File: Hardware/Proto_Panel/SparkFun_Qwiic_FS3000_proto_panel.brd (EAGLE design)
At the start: 25.4 x 25.4 mm, 58 parts, among them J2 QWIIC_RA, J3 QWIIC_RA, U1 FS3000

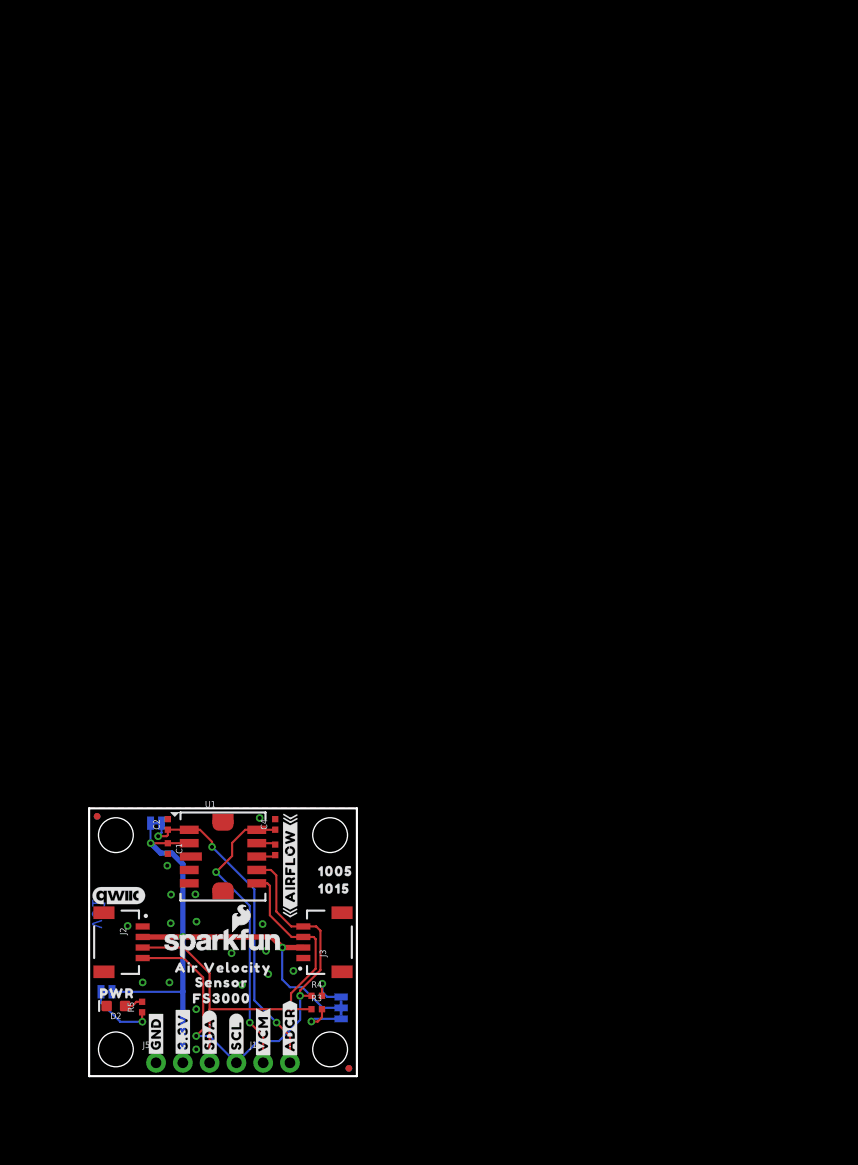
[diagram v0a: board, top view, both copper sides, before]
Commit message: Proto panel and gerbers
-Made a proto panel that includes 3 copies of each design. This allows us to order a single stencil and saves production time when building 3 prototype copies of each (1X1 and TEE) by hand.
-note, I had to move the VCM and ADCR buzzard labels on the 1x1 to a separate library, so I could drop it into the "proto panel" without it updating/breaking the other design.
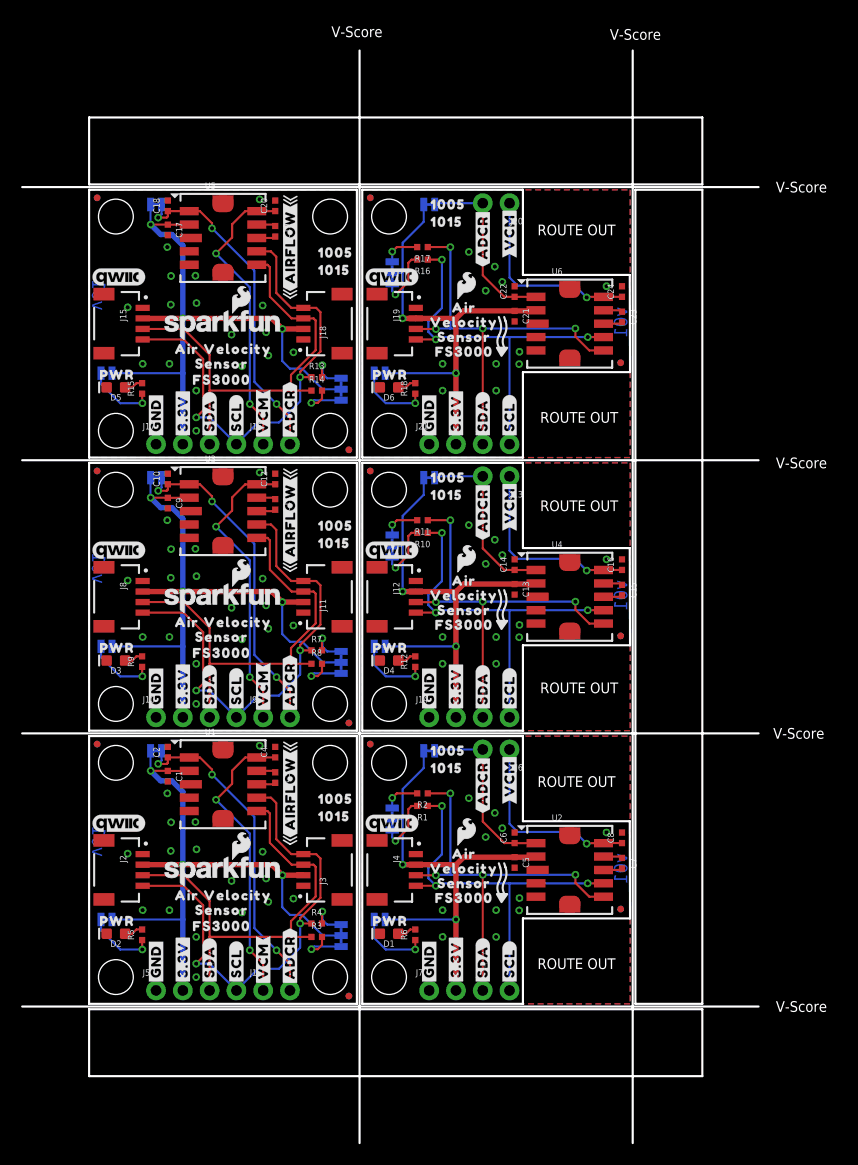
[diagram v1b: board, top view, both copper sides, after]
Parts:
- removed FRAME1: FRAME-LETTER, SparkFun-Aesthetics:CREATIVE_COMMONS
- added ADC-REF1, ADC-REF2, ADC-REF3, ADC-REF4, ADC-REF5: (no value), SparkFun-Jumpers:SMT-JUMPER_2_NC_TRACE_SILK
- added C10, C11, C13, C14, C15, C17, C18, C19, C21, C22, C23, C5, C6, C7, C9: 0.1uF, SparkFun-Capacitors:0402-TIGHT
- added C12, C16, C20, C24, C8: 1.0uF, SparkFun-Capacitors:0402-TIGHT
- added D1, D3, D4, D5, D6: RED, SparkFun-LED:LED-0603
- added I2C1, I2C2, I2C3, I2C4, I2C5: (no value), SparkFun-Jumpers:SMT-JUMPER_3_2-NC_TRACE_SILK
- added J10, J14, J17, J21, J7: (no value), SparkFun-Connectors:1X04_NO_SILK
- added J11, J12, J15, J18, J19, J4, J8: QWIIC_RA, SparkFun-Connectors:JST04_1MM_RA
- added J13, J16, J20, J6, J9: (no value), SparkFun-Connectors:1X02_NO_SILK
- added JP10, JP12, JP13, JP14, JP18, JP19, JP20, JP21, JP27, JP28, JP29, JP30, JP34, JP35, JP36, JP37, JP43, JP44, JP45, JP46: FIDUCIALUFIDUCIAL, SparkFun-Aesthetics:FIDUCIAL-MICRO
- added JP15, JP17, JP22, JP24, JP25, JP26, JP31, JP33, JP38, JP40, JP41, JP42, JP47, JP9: STAND-OFF, SparkFun-Hardware:STAND-OFF
- added JP16, JP23, JP32, JP39, JP48: LED, SparkFun-Jumpers:SMT-JUMPER_2_NC_TRACE_SILK
- added LOGO10, LOGO14, LOGO18, LOGO22, LOGO6: QWIIC_LOGO_5MM, SparkFun-Aesthetics:QWIIC_5MM
- added LOGO11, LOGO12, LOGO16, LOGO19, LOGO20, LOGO24, LOGO8: SFE_LOGO_NAME_FLAME.1_INCH, SparkFun-Aesthetics:SFE_LOGO_NAME_FLAME_.1
- added LOGO13, LOGO17, LOGO2, LOGO21, LOGO9: OSHW-LOGOMINI, SparkFun-Aesthetics:OSHW-LOGO-MINI
- added LOGO15, LOGO23, LOGO7: SFE_LOGO_FLAME.1_INCH, SparkFun-Aesthetics:SFE_LOGO_FLAME_.1
- added R1, R10, R11, R13, R14, R16, R17, R2, R7, R8: 2.2k, SparkFun-Resistors:0402-TIGHT
- added R12, R15, R18, R6, R9: 1k, SparkFun-Resistors:0402-TIGHT
- added U$1, U$113, U$114, U$142, U$143, U$2, U$57, U$58, U$86, U$87: (no value), output:#GND#0
- added U$100, U$152, U$156, U$40, U$44, U$96: (no value), output:#ADCR#0
- added U$101, U$106, U$124, U$129, U$157, U$162, U$45, U$50, U$68, U$73: (no value), output:FS30001
- added U$102, U$107, U$125, U$130, U$158, U$163, U$46, U$51, U$69, U$74: (no value), output:VELOCITY30003
- added U$103, U$108, U$126, U$131, U$159, U$164, U$47, U$52, U$70, U$75: (no value), output:AIR30004
- added U$104, U$109, U$127, U$132, U$160, U$165, U$48, U$53, U$71, U$76: (no value), output:SENSOR30005
- added U$105, U$128, U$161, U$49, U$72: (no value), output:#ADC#REF#0
- added U$110, U$136, U$166, U$54, U$80: (no value), output:10050
- added U$111, U$137, U$167, U$55, U$81: (no value), output:10150
- added U$112, U$168, U$56: (no value), output:I2C_ADR#_0X280
- added U$115, U$116, U$144, U$145, U$32, U$33, U$59, U$60, U$88, U$89: (no value), output:#3#3V#0
- added U$117, U$123, U$146, U$154, U$34, U$42, U$61, U$67, U$90, U$98: (no value), output:#SDA#0
- added U$118, U$122, U$147, U$153, U$35, U$41, U$62, U$66, U$91, U$97: (no value), output:#SCL#0
- added U$119, U$148, U$36, U$63, U$92: (no value), output:#LED#0
- added U$120, U$149, U$37, U$64, U$93: (no value), output:PWR0
- added U$121, U$150, U$38, U$65, U$94: (no value), output:#I2C#0
- added U$133, U$134, U$77, U$78: (no value), output:#AIRFLOW#0
- added U$135, U$79: (no value), output:I2C_ADD#_0X280
- added U$138, U$139, U$82, U$83: (no value), FS3000:#ADCR#4
- added U$140, U$141, U$84, U$85: (no value), FS3000:#VCM#3
- added U$151, U$155, U$39, U$43, U$95, U$99: (no value), output:#VCM#0
- added U2, U3, U4, U5, U6: FS3000, FS3000:FS3000
- moved U$28 6.86 mm to (19.2, 20.6)
- moved ADC-REF 6.86 mm to (6.35, 30.9)
- moved C1 6.86 mm to (7.47, 28.4)
- moved C2 6.86 mm to (7.47, 30.7)
- moved C3 6.86 mm to (17.7, 28.3)
- moved C4 6.86 mm to (17.7, 30.7)
- moved D2 6.86 mm to (2.54, 13.5)
- moved I2C 6.86 mm to (23.9, 13.3)
- moved J1 6.86 mm to (16.5, 8.13)
- moved J2 6.86 mm to (5.08, 19.6)
- moved J3 6.86 mm to (20.3, 19.6)
- moved J5 6.86 mm to (6.35, 8.13)
- moved JP1 6.86 mm to (1.65, 14.9)
- moved JP3 6.86 mm to (2.54, 29.7)
- moved JP4 6.86 mm to (22.9, 29.7)
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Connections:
- new net 3.3V1: ADC-REF1.1, C5.1, I2C1.2, J4.2, J7.2, JP16.2, U2.2
- new net 3.3V2: ADC-REF2.1, C9.1, I2C2.2, J10.2, J11.2, J8.2, JP23.2, U3.2
- new net 3.3V3: ADC-REF3.1, C13.1, I2C3.2, J12.2, J14.2, JP32.2, U4.2
- new net 3.3V4: ADC-REF4.1, C17.1, I2C4.2, J15.2, J17.2, J18.2, JP39.2, U5.2
- new net 3.3V5: ADC-REF5.1, C21.1, I2C5.2, J19.2, J21.2, JP48.2, U6.2
- new net ADC-REF1: ADC-REF1.2, C6.1, J6.2, U2.1
- new net ADC-REF2: ADC-REF2.2, C10.1, J9.2, U3.1
- new net ADC-REF3: ADC-REF3.2, C14.1, J13.2, U4.1
- new net ADC-REF4: ADC-REF4.2, C18.1, J16.2, U5.1
- new net ADC-REF5: ADC-REF5.2, C22.1, J20.2, U6.1
- new net GND1: C5.2, C6.2, C8.2, D1.C, J4.1, J7.1, U2.3
- new net GND2: C10.2, C12.2, C9.2, D3.C, J10.1, J11.1, J8.1, U3.3
- new net GND3: C13.2, C14.2, C16.2, D4.C, J12.1, J14.1, U4.3
- new net GND4: C17.2, C18.2, C20.2, D5.C, J15.1, J17.1, J18.1, U5.3
- new net GND5: C21.2, C22.2, C24.2, D6.C, J19.1, J21.1, U6.3
- new net N$10: JP16.1, R6.1
- new net N$11: C7.1, U2.9
- new net N$12: C7.2, U2.8
- new net N$13: I2C2.1, R8.2
- new net N$14: I2C2.3, R7.2
- new net N$15: D3.A, R9.2
- new net N$16: JP23.1, R9.1
- new net N$17: C11.1, U3.9
- new net N$18: C11.2, U3.8
- new net N$19: I2C3.1, R11.2
- new net N$20: I2C3.3, R10.2
- new net N$21: D4.A, R12.2
- new net N$22: JP32.1, R12.1
- new net N$23: C15.1, U4.9
- new net N$24: C15.2, U4.8
- new net N$25: I2C4.1, R14.2
- new net N$26: I2C4.3, R13.2
- new net N$27: D5.A, R15.2
- new net N$28: JP39.1, R15.1
- new net N$29: C19.1, U5.9
- new net N$30: C19.2, U5.8
- new net N$31: I2C5.1, R17.2
- new net N$32: I2C5.3, R16.2
- new net N$33: D6.A, R18.2
- new net N$34: JP48.1, R18.1
- new net N$35: C23.1, U6.9
- new net N$36: C23.2, U6.8
- new net N$5: I2C1.1, R2.2
- new net N$7: I2C1.3, R1.2
- new net N$9: D1.A, R6.2
- new net SCL1: J4.4, J7.4, R1.1, U2.7
- new net SCL2: J10.4, J11.4, J8.4, R7.1, U3.7
- new net SCL3: J12.4, J14.4, R10.1, U4.7
- new net SCL4: J15.4, J17.4, J18.4, R13.1, U5.7
- new net SCL5: J19.4, J21.4, R16.1, U6.7
- new net SDA1: J4.3, J7.3, R2.1, U2.6
- new net SDA2: J10.3, J11.3, J8.3, R8.1, U3.6
- new net SDA3: J12.3, J14.3, R11.1, U4.6
- new net SDA4: J15.3, J17.3, J18.3, R14.1, U5.6
- new net SDA5: J19.3, J21.3, R17.1, U6.6
- new net VCM1: C8.1, J6.1, U2.10
- new net VCM2: C12.1, J9.1, U3.10
- new net VCM3: C16.1, J13.1, U4.10
- new net VCM4: C20.1, J16.1, U5.10
- new net VCM5: C24.1, J20.1, U6.10
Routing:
- net 3.3V4: track 0.00 -> 60.4 mm, vias 0 -> 3
- net 3.3V2: track 0.00 -> 60.4 mm, vias 0 -> 3
- net SCL2: track 0.00 -> 45.7 mm, vias 0 -> 2
- net SCL4: track 0.00 -> 45.7 mm, vias 0 -> 2
- net 3.3V5: track 0.00 -> 44.2 mm, vias 0 -> 2
- net 3.3V1: track 0.00 -> 44.2 mm, vias 0 -> 2
- net 3.3V3: track 0.00 -> 44.2 mm, vias 0 -> 2
- net SDA2: track 0.00 -> 42.5 mm
- net SDA4: track 0.00 -> 42.5 mm
- net SDA3: track 0.00 -> 40.0 mm, vias 0 -> 4
- net SDA5: track 0.00 -> 40.0 mm, vias 0 -> 4
- net SDA1: track 0.00 -> 40.0 mm, vias 0 -> 4
- net SCL5: track 0.00 -> 37.8 mm, vias 0 -> 3
- net SCL3: track 0.00 -> 37.8 mm, vias 0 -> 3
- net SCL1: track 0.00 -> 37.8 mm, vias 0 -> 3
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- added copper zone on layer 1, net GND1
- added copper zone on layer 16, net GND1
- added copper zone on layer 1, net GND2
- added copper zone on layer 16, net GND2
- added copper zone on layer 1, net GND3
- added copper zone on layer 16, net GND3
- added copper zone on layer 1, net GND4
- added copper zone on layer 16, net GND4
- added copper zone on layer 1, net GND5
- added copper zone on layer 16, net GND5
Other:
- board size 25.4 x 25.4 mm -> 69.8 x 103.6 mm
- board text added: "ROUTE OUT"
- board text added: "V-Score"
- board text removed: "Measure Units: INCHES"
- board text removed: "Pete Lewis"
